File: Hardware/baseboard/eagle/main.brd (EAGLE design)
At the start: 359.1 x 113.3 mm, 198 parts, among them J1 MICROUSB-FEM, X1 JST-4POS-2X4POS, X1.2 TACH/LAP, X2 ATLAS-LTC, X2.1 MOTOR, X2.2 VRAILS+, X2.3 5V+SoC, X5 15244441

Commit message: baseboard - cleared some comments on layout and schematic file
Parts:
- moved A6:C1 28.9 mm to (20.3, 31.8)
- moved A10:C1 6.24 mm to (42.4, 51.1), turned to 180 degrees
- moved A10:R1 3.41 mm to (41.6, 49.4)
- moved A10:R2 3.08 mm to (45.7, 49.4), turned to 90 degrees
- moved A10:R7 2.21 mm to (44.0, 48.7), turned to 270 degrees
- moved A5:C5 1.12 mm to (34.1, 44.3)
- moved A10:R3 0.57 mm to (36.4, 50.6)
- moved A5:R5 0.09 mm to (22.4, 49.1)
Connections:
- net +18V: now also SV2.3; no longer SV2.2
- net +4.1V: now also SV2.2; no longer SV2.3
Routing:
- net A10:HYST: track 7.03 -> 0.00 mm
- net +5V: track 52.5 -> 58.9 mm
- net A6:TRACK/SS: track 7.98 -> 1.92 mm, vias 1 -> 0
- net A10:BATOK: track 6.41 -> 11.3 mm, vias 0 -> 1
- net +3V3: track 74.6 -> 71.4 mm, vias 5 -> 4
- net A10:REF: track 3.17 -> 0.00 mm
- net VDD: track 80.7 -> 79.0 mm, vias 10 -> 9
- net A10:COMP: track 1.56 -> 0.00 mm
- net +4.1V: track 78.9 -> 77.7 mm, vias 5 -> 6
- net TOP.MODE: track 29.2 -> 30.4 mm
- net SYSTWI.SCL: track 146.8 -> 145.8 mm
- net SYSTWI.SDA: track 147.2 -> 146.2 mm
- net TOP.RUN: track 22.9 -> 22.1 mm
- net A5:IIMON: track 3.61 -> 4.30 mm
- net A6:↔ILIM: track 23.4 -> 22.8 mm
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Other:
- board text added: "!INT! auf inneren Layer"
- board text added: "DIFF REFACTOR"
- board text added: "Double trace width"
- board text added: "GPIO REIN!"
- board text added: "ROOM"
- board text added: "TODO: Find +18V route when space is left after airwiring is done"
- board text removed: "Center Area: - Gyroscope (top) - Managment GPIO (bottom)"
- board text removed: "DOUBLE UP!"
- board text removed: "E.Z"
- board text removed: "Size less than credit card by the way. Fuck me."
- board text removed: "almost forgot"
- board text removed: "along with the I2C"
- board text removed: "it's many small vias eating away board area and producing slot antennas and other sheister I am not willing to consider or 1 via with a massive copper rod through it worth 10 vias is what I'm getting at anyone arguning that this is overcomplicating the desingn, please read again."
- board text removed: "same maneuver regarding powerlines as seen at other connectors, add \!!sparse!\! gumstick-type pinhead landing (refer to original svg) for free vias capable of carrying much power (+I2C et al of course)"
- board text removed: "solder bridges are missing"

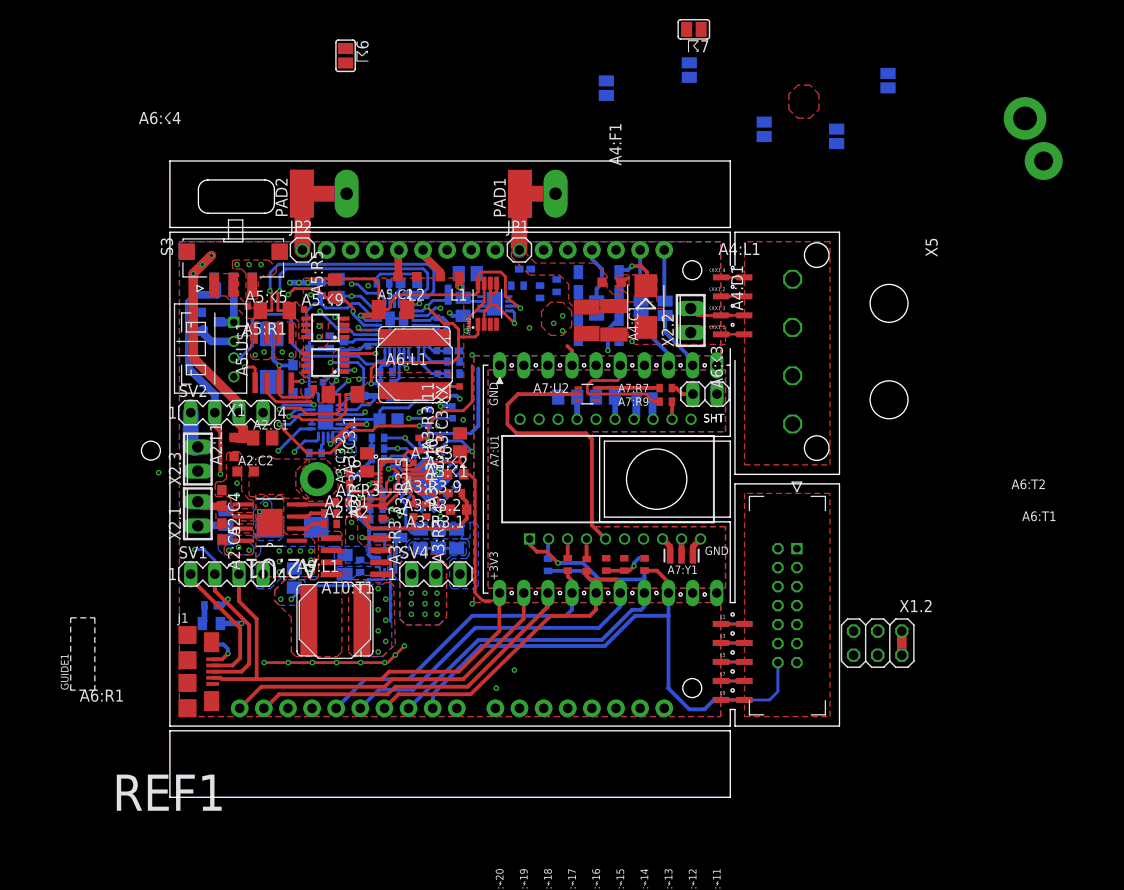
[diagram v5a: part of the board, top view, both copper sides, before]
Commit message: wip baseboard 45 airwires, resolved some conflicts
this is an exponential progress, the last 50 wires seem the hardest
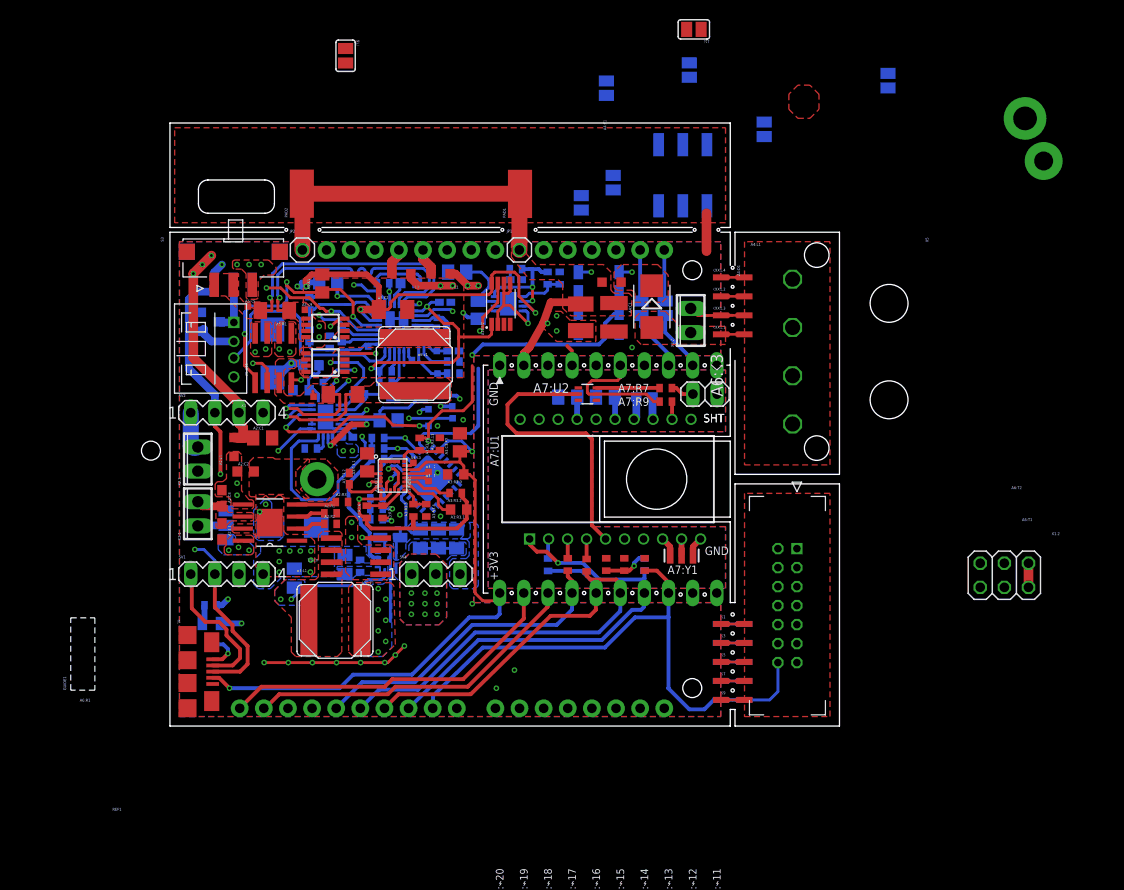
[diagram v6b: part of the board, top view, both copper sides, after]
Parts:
- removed A6:☇4: PTR1TP07SQ, testpad:TP07SQ
- removed F2: (no value), fuse:SH22
- added S4: 219-03J, switch-dil:CTS-219-03J
- moved ☈2 27.8 mm to (48.3, 58.1), turned to 90 degrees
- moved X1.2 15.1 mm to (92.9, 18.9)
- moved ☈3 13.3 mm to (51.7, 60.2), turned to 270 degrees
- moved A10:R7 2.51 mm to (46.0, 50.2)
- moved A5:R4 1.96 mm to (19.7, 47.5)
- moved A10:R1 1.75 mm to (41.4, 51.1), turned to 180 degrees
- moved A10:R4 1.62 mm to (37.5, 46.8)
- moved A10:C1 1.46 mm to (41.4, 50.0)
- moved A5:R5 1.46 mm to (21.0, 49.6)
- moved A10:U1 1.43 mm to (40.6, 47.5)
- moved A10:U2 1.43 mm to (39.8, 47.5)
- moved A10:R2 1.24 mm to (44.8, 50.2), turned to 270 degrees
- moved A5:R3 1.15 mm to (21.7, 49.7), turned to 180 degrees
- moved A10:R3 1.12 mm to (35.2, 50.8), turned to 180 degrees
- moved A6:R2 1.03 mm to (19.8, 41.0)
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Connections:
- removed net TOP.18V/PREFUSE: A4:C1.1, A4:F1.1, A4:L1.2, A4:R3.2, F2.1, JP1.1, PAD1.1
- net +18V: now also A4:C1.1, A4:F1.1, A4:L1.2, A4:R3.2, JP1.1, PAD1.1; no longer F2.2
- net A6:~SENSE+: no longer A6:☇4.TP
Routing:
- net +18V: track 47.3 -> 82.2 mm
- net SYSTWI.SDA: track 146.2 -> 122.2 mm
- net TOP.RRX: track 45.6 -> 59.0 mm, vias 3 -> 2
- net SYSTWI.!INT: track 79.3 -> 67.2 mm, vias 1 -> 2
- net A10:REF: track 0.00 -> 11.9 mm, vias 0 -> 2
- net TOP.OS1IS2: track 31.6 -> 21.5 mm
- net +4.1V: track 77.7 -> 87.5 mm, vias 6 -> 7
- net TOP.18V/PREFUSE: track 9.68 -> 1.59 mm, vias 0 -> 1
- net TOP.FREQ: track 23.5 -> 31.2 mm
- net A4:N$1: track 8.68 -> 2.57 mm
- net UNO.ADC2: track 6.01 -> 0.00 mm
- net TOP.PGOOD: track 28.0 -> 23.1 mm
- net A10:HYST: track 0.00 -> 4.84 mm
- net VDD: track 79.0 -> 83.8 mm, vias 9 -> 8
- net A6:~SENSE+: track 4.96 -> 0.63 mm
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- added copper zone on layer 1, net +18V
- added copper zone on layer 15, net TOP.MOT-
- removed copper zone on layer 1, net TOP.18V/PREFUSE
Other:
- outline, holes or cut-outs redrawn
- board text added: "(A) PLACE CONNECTOR TO HERE"
- board text added: "MOVE CONNECTOR TO (A)"
- board text removed: "DIFF REFACTOR"
- board text removed: "TODO LATR"

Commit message: wip baseboard layout
just open it if you want to see the changes who even cares
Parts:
- removed X5: 15244441, kitt.con:MOLEX_15244441
- removed ☇1: 1, kitt.con:CON.BUOC.BREAKPAD-P5MM
- removed ☇10: 10, kitt.con:CON.BUOC.BREAKPAD-P5MM
- removed ☇2: 2, kitt.con:CON.BUOC.BREAKPAD-P5MM
- removed ☇3: 3, kitt.con:CON.BUOC.BREAKPAD-P5MM
- removed ☇4: 4, kitt.con:CON.BUOC.BREAKPAD-P5MM
- removed ☇5: 5, kitt.con:CON.BUOC.BREAKPAD-P5MM
- removed ☇6: 6, kitt.con:CON.BUOC.BREAKPAD-P5MM
- removed ☇7: 7, kitt.con:CON.BUOC.BREAKPAD-P5MM
- removed ☇8: 8, kitt.con:CON.BUOC.BREAKPAD-P5MM
- removed ☇9: 9, kitt.con:CON.BUOC.BREAKPAD-P5MM
- removed ☇XX1.1: VRAILS, kitt.con:CON.BUOC.BREAKPAD-P5MM
- removed ☇XX1.2, ☇XX1.3: GND, kitt.con:CON.BUOC.BREAKPAD-P5MM
- removed ☇XX1.4: +5V, kitt.con:CON.BUOC.BREAKPAD-P5MM
- removed ☈1, ☈6, ☈9: (no value), jumper:SJ
- added L3: BEAD/0R/⎵, rcl:L2012C
- A6:☇6, A6:☇7, A6:☇8, A6:☇9: value PTR1TP07SQ -> PTR1TP07R; device testpad:TP07SQ -> testpad:TP07R
- moved X2 48.3 mm to (21.8, 14.3), turned to 180 degrees
- moved S4 48.1 mm to (107.0, 64.5)
- moved X1.2 33.7 mm to (60.2, 27.2), turned to 180 degrees
- moved A7:⌁2 19.0 mm to (52.4, 57.0)
- moved A7:⌁6 19.0 mm to (42.3, 57.0)
- moved ☈10 18.7 mm to (54.8, 65.7)
- moved ☈11 18.7 mm to (57.1, 65.7)
- moved A4:F1 18.3 mm to (47.0, 64.3), turned to 180 degrees
- moved A4:R4 17.0 mm to (49.7, 62.4), turned to 0 degrees
- moved A10:C1 17.0 mm to (38.3, 66.7), turned to 0 degrees
- moved A7:⌁3 16.8 mm to (49.9, 57.0)
- moved A4:L1 16.8 mm to (51.8, 66.5)
- moved X2.2 16.7 mm to (61.0, 62.3)
- moved A6:☇6 16.4 mm to (33.3, 51.7)
- moved A5:R3 16.3 mm to (21.4, 66.0)
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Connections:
- removed net A7:!RESET: A7:R9.2, A7:U2.5, A7:⌁6.P$1
- removed net UNO.ADC0: XA1.ADC.0, ☈1.2
- removed net VSYS: A7:⌁3.P$1, ☈2.1
- net !CS1: no longer ☇10.X1
- net +5V: no longer X5.4, ☇XX1.4.X1
- net GND: no longer X5.2, X5.3, ☇XX1.2.X1, ☇XX1.3.X1
- net SYSTWI.!INT: now also A8:IC1.15
- net TOP.!RST: now also A7:R9.2, A7:U2.5, A7:⌁6.P$1
- net TOP.FREQ: now also A8:IC1.19
- net TOP.MODE: now also A8:IC1.18
- net TOP.MVPRW: now also ☈3.1; no longer ☈1.1
- net TOP.PGOOD: now also A8:IC1.20
- net TOP.RUN: now also A8:IC1.17
- net UNO.3V3: now also L3.1
- net UNO.ADC3: no longer ☈9.2
- net UNO.IOREF: now also L3.2; no longer ☈6.2
- net VCC/2: no longer X5.1, ☇XX1.1.X1
- net VDD: now also A7:⌁3.P$1, ☈2.1
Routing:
- net VDD: track 83.8 -> 43.3 mm, vias 8 -> 9
- net SYSTWI.SCL: track 148.9 -> 119.8 mm
- net UNO.RESET: track 0.00 -> 28.5 mm
- net SYSTWI.SDA: track 122.2 -> 93.8 mm
- net !CS1: track 60.0 -> 35.6 mm
- net +5V: track 57.8 -> 40.9 mm, vias 3 -> 4
- net TOP.!RST: track 13.9 -> 30.0 mm
- net +18V: track 82.2 -> 97.1 mm
- net +3V3: track 75.1 -> 89.8 mm
- net A7:!RESET: track 13.9 -> 0.00 mm
- net SYSTWI.!INT: track 67.2 -> 81.0 mm
- net TOP.RRX: track 59.0 -> 47.7 mm, vias 2 -> 4
- net GND: track 56.0 -> 48.7 mm, vias 36 -> 33
- net TOP.FREQ: track 31.2 -> 37.5 mm
- net A6:↔ILIM: track 23.0 -> 16.9 mm, vias 3 -> 2
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- added copper zone on layer 16, net A5:IGATE
- added copper zone on layer 16, net A6:SW✳
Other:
- board size 359.1 x 113.3 mm -> 359.1 x 123.5 mm
- board text removed: "!INT! auf inneren Layer"
- board text removed: "-> TI's got it down, look up their ref design: think altpart compatible landing pattern"
- board text removed: "A BUNCH OF WIRES"
- board text removed: "AREA 3: LOGIC"
- board text removed: "ATLAS LTC"
- board text removed: "Double trace width"
- board text removed: "EDU LIMIT"
- board text removed: "GPIO REIN!"
- board text removed: "MOVE CONNECTOR TO (A)"
- board text removed: "TODO for final phase: Add stopmask extension for all inductors"

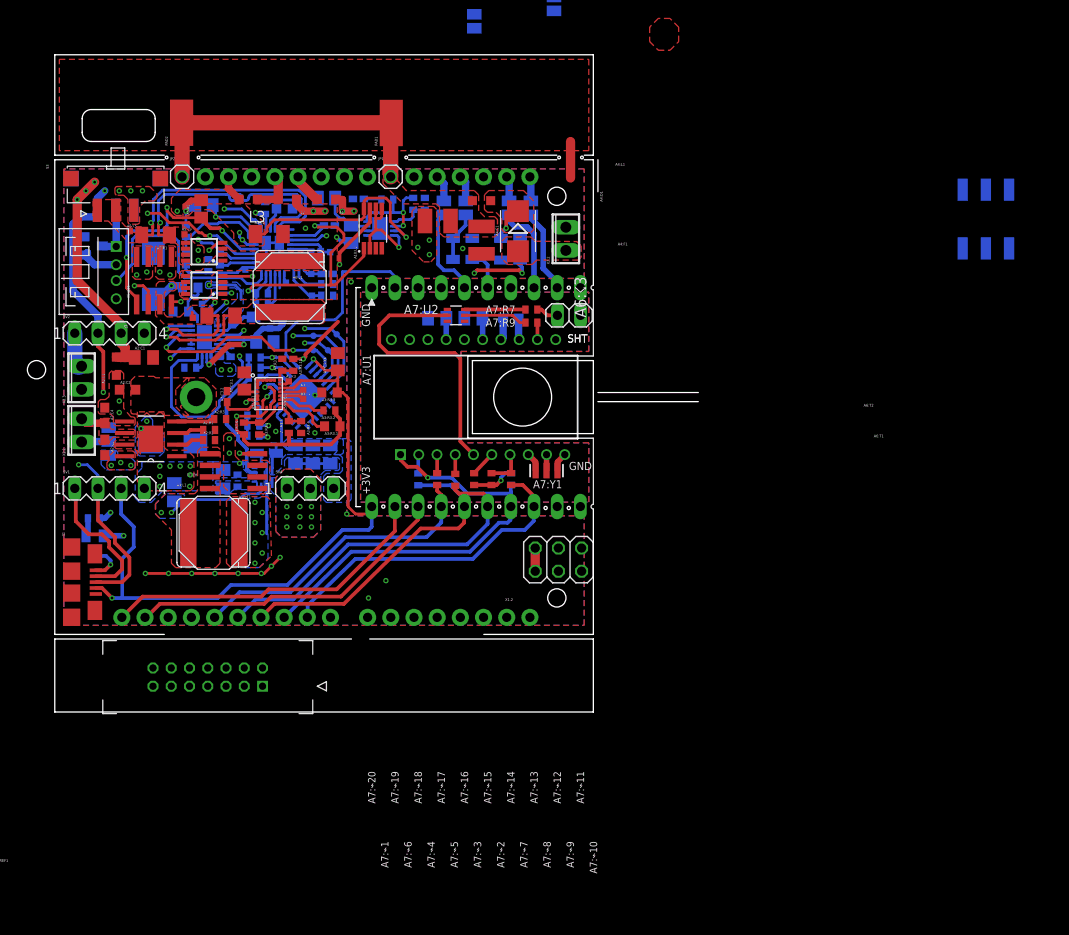
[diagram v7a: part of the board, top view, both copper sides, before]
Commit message: baseboard layout: dropped LTC connector -> we do not need a specialized layout for that
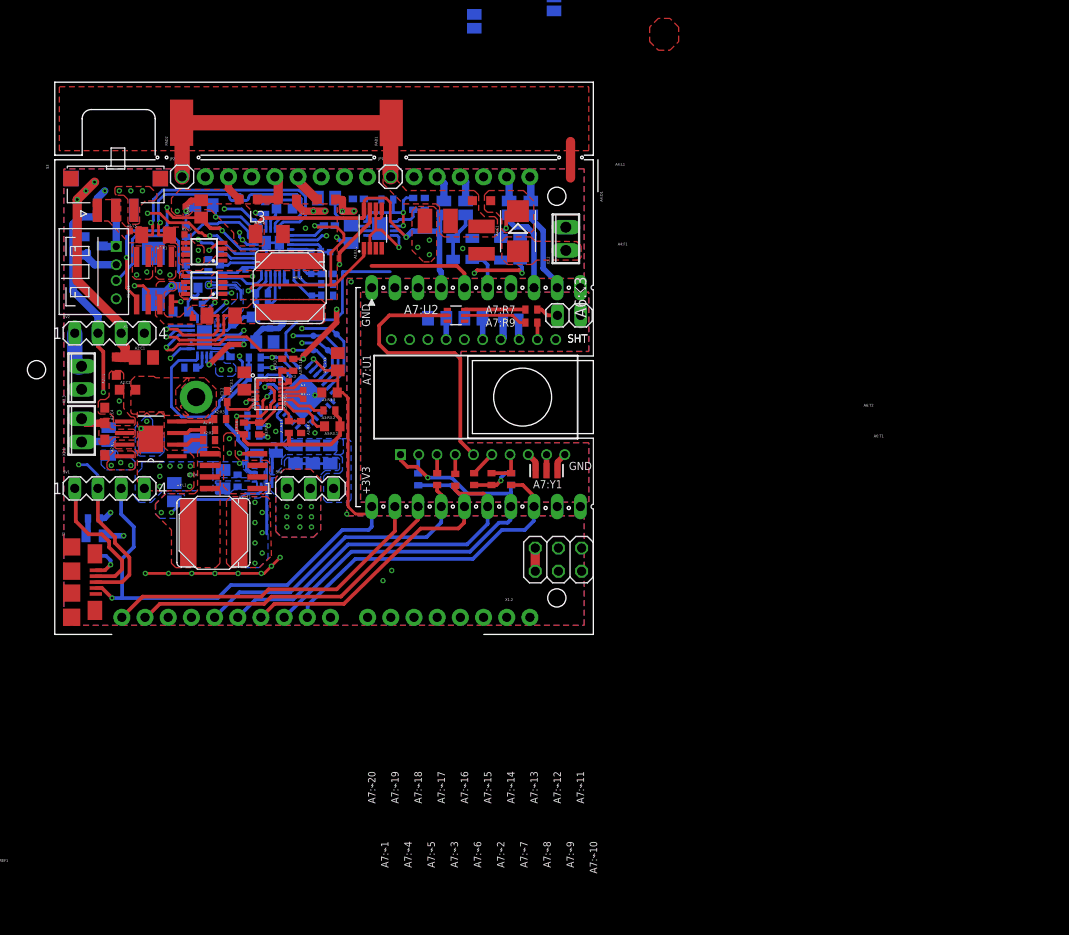
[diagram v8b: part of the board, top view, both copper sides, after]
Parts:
- removed S4: 219-03J, switch-dil:CTS-219-03J
- removed X2: ATLAS-LTC, kitt.con:LTC-CONNECTOR
- moved A7:⌁6 7.62 mm to (49.9, 57.0)
- moved A7:⌁5 2.54 mm to (44.8, 57.0)
- moved A7:⌁3 2.54 mm to (47.3, 57.0)
- moved A7:⌁4 2.54 mm to (42.3, 57.0)
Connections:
- net !CS1: no longer X2.14
- net +3V3: no longer X2.10, X2.2
- net +9V: no longer X2.1
- net GND: no longer X2.12, X2.13, X2.3, X2.7, X2.8
- net MISO: no longer X2.5
- net MOSI: no longer X2.6
- net SYSTWI.SCL: no longer X2.11
- net SYSTWI.SDA: no longer X2.9
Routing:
- net TOP.RRX: track 47.7 -> 35.5 mm
- net +5V: track 40.9 -> 52.8 mm
- net TOP.!RST: track 30.0 -> 40.1 mm
- net SYSTWI.SCL: track 119.8 -> 116.7 mm
- net +3V3: track 89.8 -> 92.3 mm, vias 6 -> 7
- net VDD: track 43.3 -> 45.7 mm
- net SYSTWI.SDA: track 93.8 -> 91.8 mm
- net UNO.RESET: track 28.5 -> 27.1 mm
- net TOP.MODE: track 27.4 -> 28.5 mm
- net TOP.PGOOD: track 26.1 -> 25.4 mm
- net TOP.FREQ: track 37.5 -> 38.1 mm
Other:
- board size 359.1 x 123.5 mm -> 359.1 x 120.5 mm
- board text removed: "(A) PLACE CONNECTOR TO HERE"
- board text removed: "182 airwires? i don't give a rats' nest."
- board text removed: "< change index mark to bottom, next to pin"
- board text removed: "REPLACE \w HOOK-IN VIA"
- board text removed: "useful: https://technick.net/tools/impedance-calculator/microstrip/"
